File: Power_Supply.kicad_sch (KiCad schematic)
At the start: 24 parts, among them J1 Barrel_Jack, Q25 KSP2907A, Q26 IRF644, SW1 PB400EEQX, U1 L7805, U2 MC34063AP

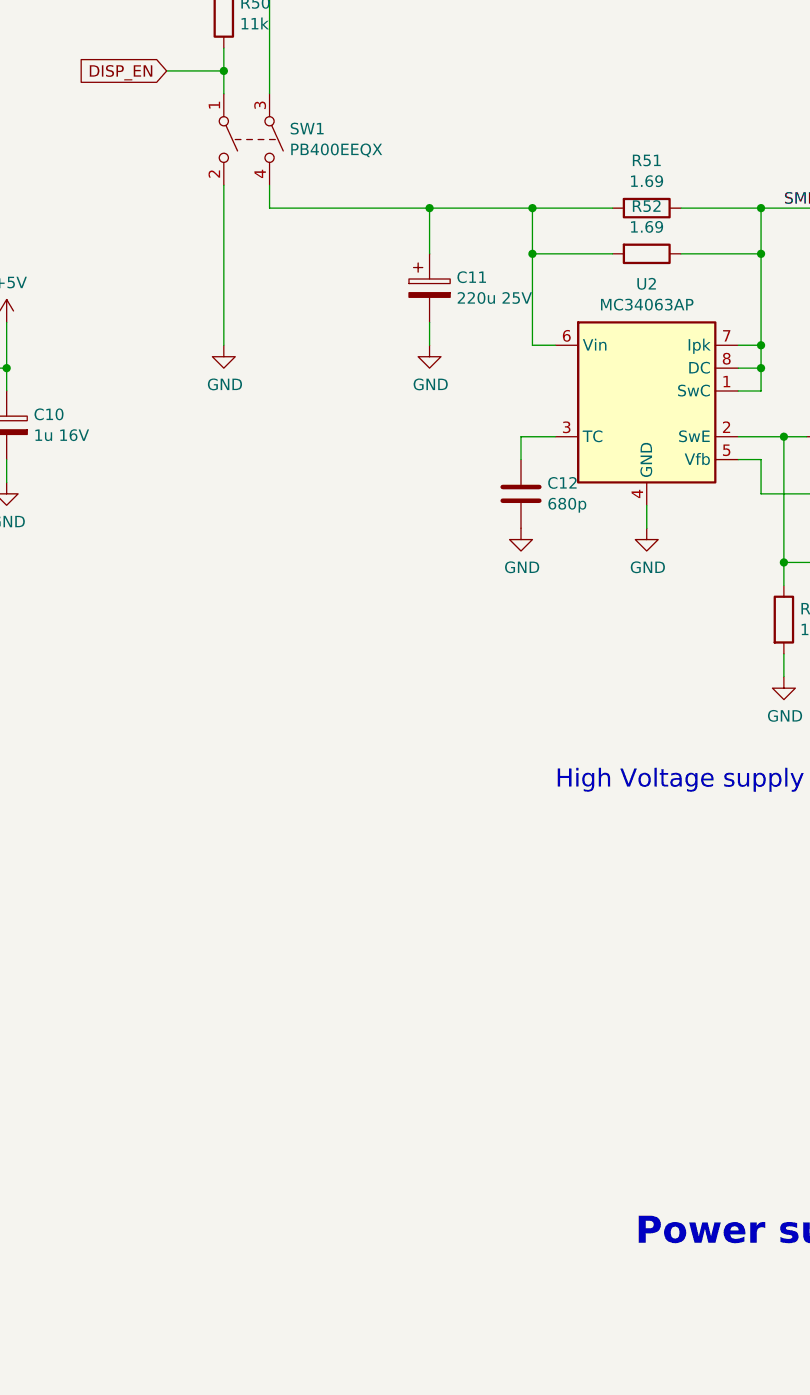
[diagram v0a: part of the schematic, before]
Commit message: Implemented changes from pablo_cambios branch. Generated Gerbers
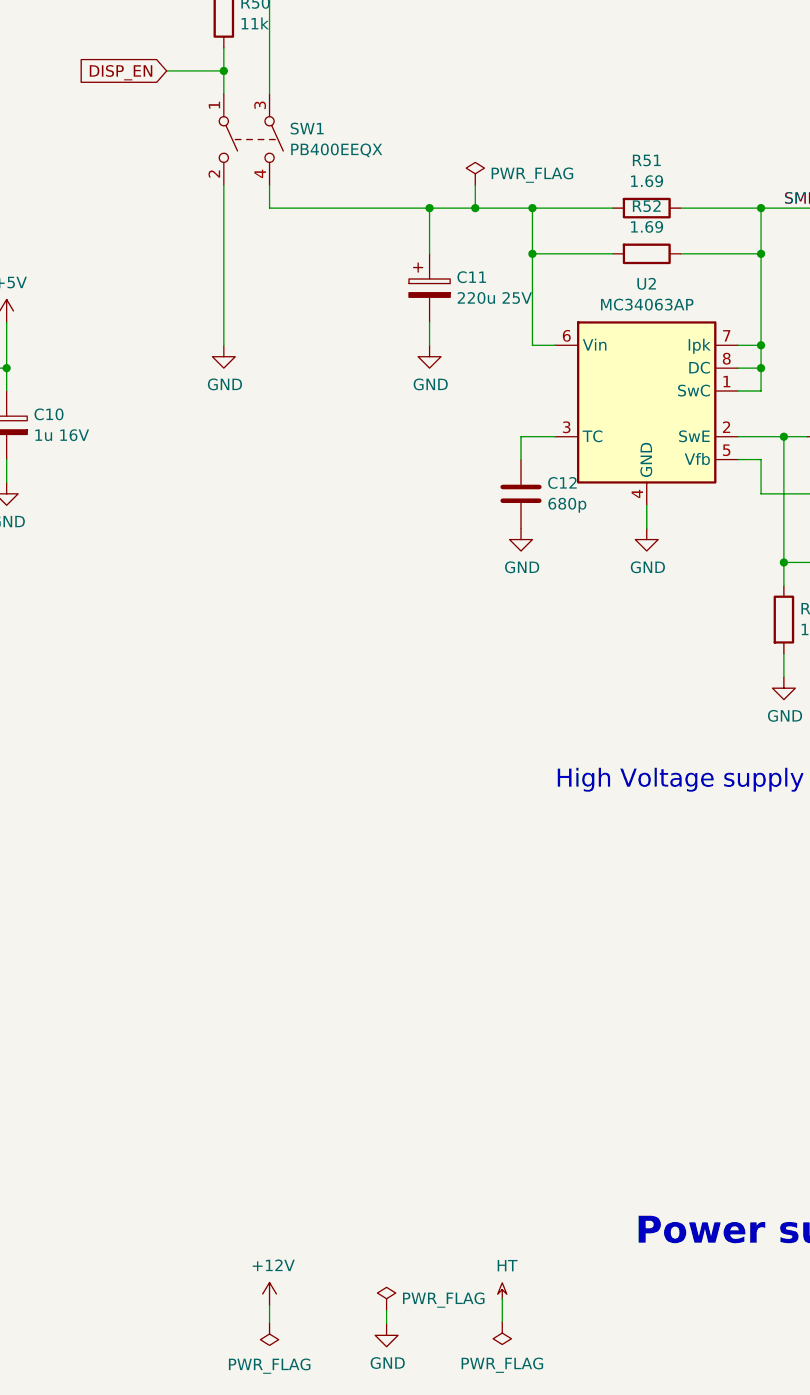
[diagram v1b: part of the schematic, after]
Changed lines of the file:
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@@
   (junction (at 194.31 76.2) (diameter 0) (color 0 0 0 0)
   )
+  (junction (at 162.56 60.96) (diameter 0) (color 0 0 0 0)
+  )
   (junction (at 157.48 60.96) (diameter 0) (color 0 0 0 0)
   )
@@
     (stroke (width 0) (type default) (color 0 0 0 0))
   )
+  (wire (pts (xy 139.7 182.88) (xy 139.7 184.785))
+    (stroke (width 0) (type default) (color 0 0 0 0))
+  )
   (wire (pts (xy 240.03 90.17) (xy 240.03 92.71))
     (stroke (width 0) (type default) (color 0 0 0 0))
@@
     (stroke (width 0) (type default) (color 0 0 0 0))
   )
+  (wire (pts (xy 152.7048 183.4134) (xy 152.7048 184.9374))
+    (stroke (width 0) (type default) (color 0 0 0 0))
+  )
   (wire (pts (xy 194.31 66.04) (xy 194.31 60.96))
     (stroke (width 0) (type default) (color 0 0 0 0))
@@
     (stroke (width 0) (type default) (color 0 0 0 0))
   )
-  (wire (pts (xy 157.48 60.96) (xy 168.91 60.96))
+  (wire (pts (xy 157.48 60.96) (xy 162.56 60.96))
     (stroke (width 0) (type default) (color 0 0 0 0))
   )
@@
     (stroke (width 0) (type default) (color 0 0 0 0))
   )
+  (wire (pts (xy 162.56 58.42) (xy 162.56 60.96))
+    (stroke (width 0) (type default) (color 0 0 0 0))
+  )
+  (wire (pts (xy 165.5572 182.1434) (xy 165.5572 184.6834))
+    (stroke (width 0) (type default) (color 0 0 0 0))
+  )
   (wire (pts (xy 83.82 78.74) (xy 83.82 81.28))
     (stroke (width 0) (type default) (color 0 0 0 0))
@@
   )
   (wire (pts (xy 134.62 45.72) (xy 134.62 48.26))
+    (stroke (width 0) (type default) (color 0 0 0 0))
+  )
+  (wire (pts (xy 162.56 60.96) (xy 168.91 60.96))
     (stroke (width 0) (type default) (color 0 0 0 0))
   )
@@
     (pin "3")
   )
+  (symbol (lib_id "power:GND") (at 152.7048 184.9374 0) (unit 1)
+    (in_bom yes) (on_board yes)
+    (property "Reference" "#PWR0148" (id 0) (at 152.7048 191.2874 0)
+      (effects (font (size 1.27 1.27)) hide)
+    )
+    (property "Value" "GND" (id 1) (at 152.8318 189.3316 0))
+    (property "Footprint" "" (id 2) (at 152.7048 184.9374 0)
+      (effects (font (size 1.27 1.27)) hide)
+    )
+    (property "Datasheet" "" (id 3) (at 152.7048 184.9374 0)
+      (effects (font (size 1.27 1.27)) hide)
+    )
+    (pin "1")
+  )
+  (symbol (lib_id "power:PWR_FLAG") (at 152.7048 183.4134 0) (unit 1)
+    (in_bom yes) (on_board yes) (fields_autoplaced)
+    (property "Reference" "#FLG0101" (id 0) (at 152.7048 181.5084 0)
+      (effects (font (size 1.27 1.27)) hide)
+    )
+    (property "Value" "PWR_FLAG" (id 1) (at 154.3558 182.1433 0)
+      (effects (font (size 1.27 1.27)) (justify left))
+    )
+    (property "Footprint" "" (id 2) (at 152.7048 183.4134 0)
+      (effects (font (size 1.27 1.27)) hide)
+    )
+    (property "Datasheet" "~" (id 3) (at 152.7048 183.4134 0)
+      (effects (font (size 1.27 1.27)) hide)
+    )
+    (pin "1")
+  )
   (symbol (lib_id "power:GND") (at 83.82 91.44 0) (unit 1)
     (in_bom yes) (on_board yes)
@@
     (pin "1")
   )
+  (symbol (lib_id "power:PWR_FLAG") (at 162.56 58.42 0) (unit 1)
+    (in_bom yes) (on_board yes) (fields_autoplaced)
+    (property "Reference" "#FLG0104" (id 0) (at 162.56 56.515 0)
+      (effects (font (size 1.27 1.27)) hide)
+    )
+    (property "Value" "PWR_FLAG" (id 1) (at 164.211 57.1499 0)
+      (effects (font (size 1.27 1.27)) (justify left))
+    )
+    (property "Footprint" "" (id 2) (at 162.56 58.42 0)
+      (effects (font (size 1.27 1.27)) hide)
+    )
+    (property "Datasheet" "~" (id 3) (at 162.56 58.42 0)
+      (effects (font (size 1.27 1.27)) hide)
+    )
+    (pin "1")
+  )
+  (symbol (lib_id "power:PWR_FLAG") (at 139.7 184.785 180) (unit 1)
+    (in_bom yes) (on_board yes) (fields_autoplaced)
+    (property "Reference" "#FLG0102" (id 0) (at 139.7 186.69 0)
+      (effects (font (size 1.27 1.27)) hide)
+    )
+    (property "Value" "PWR_FLAG" (id 1) (at 139.7 189.484 0))
+    (property "Footprint" "" (id 2) (at 139.7 184.785 0)
+      (effects (font (size 1.27 1.27)) hide)
+    )
+    (property "Datasheet" "~" (id 3) (at 139.7 184.785 0)
+      (effects (font (size 1.27 1.27)) hide)
+    )
+    (pin "1")
+  )
   (symbol (lib_id "Device:C") (at 83.82 85.09 0) (unit 1)
     (in_bom yes) (on_board yes)
@@
     (pin "2")
   )
+  (symbol (lib_id "power:PWR_FLAG") (at 165.5572 184.6834 180) (unit 1)
+    (in_bom yes) (on_board yes) (fields_autoplaced)
+    (property "Reference" "#FLG0103" (id 0) (at 165.5572 186.5884 0)
+      (effects (font (size 1.27 1.27)) hide)
+    )
+    (property "Value" "PWR_FLAG" (id 1) (at 165.5572 189.3824 0))
+    (property "Footprint" "" (id 2) (at 165.5572 184.6834 0)
+      (effects (font (size 1.27 1.27)) hide)
+    )
+    (property "Datasheet" "~" (id 3) (at 165.5572 184.6834 0)
+      (effects (font (size 1.27 1.27)) hide)
+    )
+    (pin "1")
+  )
+  (symbol (lib_id "power:HT") (at 165.5572 182.1434 0) (unit 1)
+    (in_bom yes) (on_board yes)
+    (property "Reference" "#PWR0149" (id 0) (at 165.5572 179.0954 0)
+      (effects (font (size 1.27 1.27)) hide)
+    )
+    (property "Value" "HT" (id 1) (at 166.0652 178.5112 0))
+    (property "Footprint" "" (id 2) (at 165.5572 182.1434 0)
+      (effects (font (size 1.27 1.27)) hide)
+    )
+    (property "Datasheet" "" (id 3) (at 165.5572 182.1434 0)
+      (effects (font (size 1.27 1.27)) hide)
+    )
+    (pin "1")
+  )
+  (symbol (lib_id "power:+12V") (at 139.7 182.88 0) (unit 1)
+    (in_bom yes) (on_board yes)
+    (property "Reference" "#PWR0147" (id 0) (at 139.7 186.69 0)
+      (effects (font (size 1.27 1.27)) hide)
+    )
+    (property "Value" "+12V" (id 1) (at 140.081 178.4858 0))
+    (property "Footprint" "" (id 2) (at 139.7 182.88 0)
+      (effects (font (size 1.27 1.27)) hide)
+    )
+    (property "Datasheet" "" (id 3) (at 139.7 182.88 0)
+      (effects (font (size 1.27 1.27)) hide)
+    )
+    (pin "1")
+  )
 )
